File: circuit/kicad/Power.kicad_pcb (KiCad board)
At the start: 2 copper layers, 78.8 x 54.8 mm, 66 parts, among them J1 ILG2, J2 PA3, J3 FFC4, J4 FFC7, J5 PA2, J6 PA2, Q1 CXDM4060P, SW1 SW_DPDT_x2, SW2 220AMB16R, SW3 SKRPABE010, SW4 SKRPABE010, SW5 SKRPABE010, U1 AZ1117R-5.0TRE1, U2 AZ1117IH-3.3TRG1, U3 DRV8874, U4 DRV8874

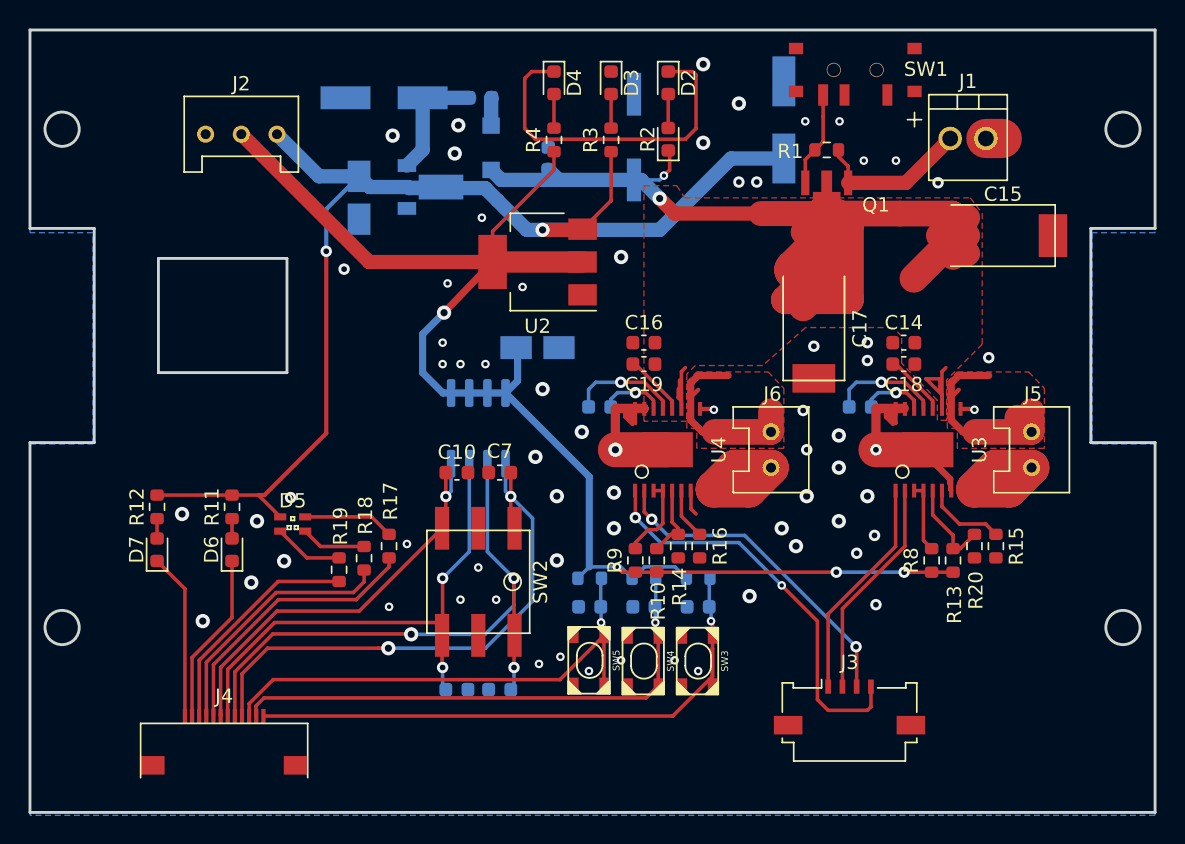
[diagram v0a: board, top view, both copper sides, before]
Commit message: フットプリントの問題は解消
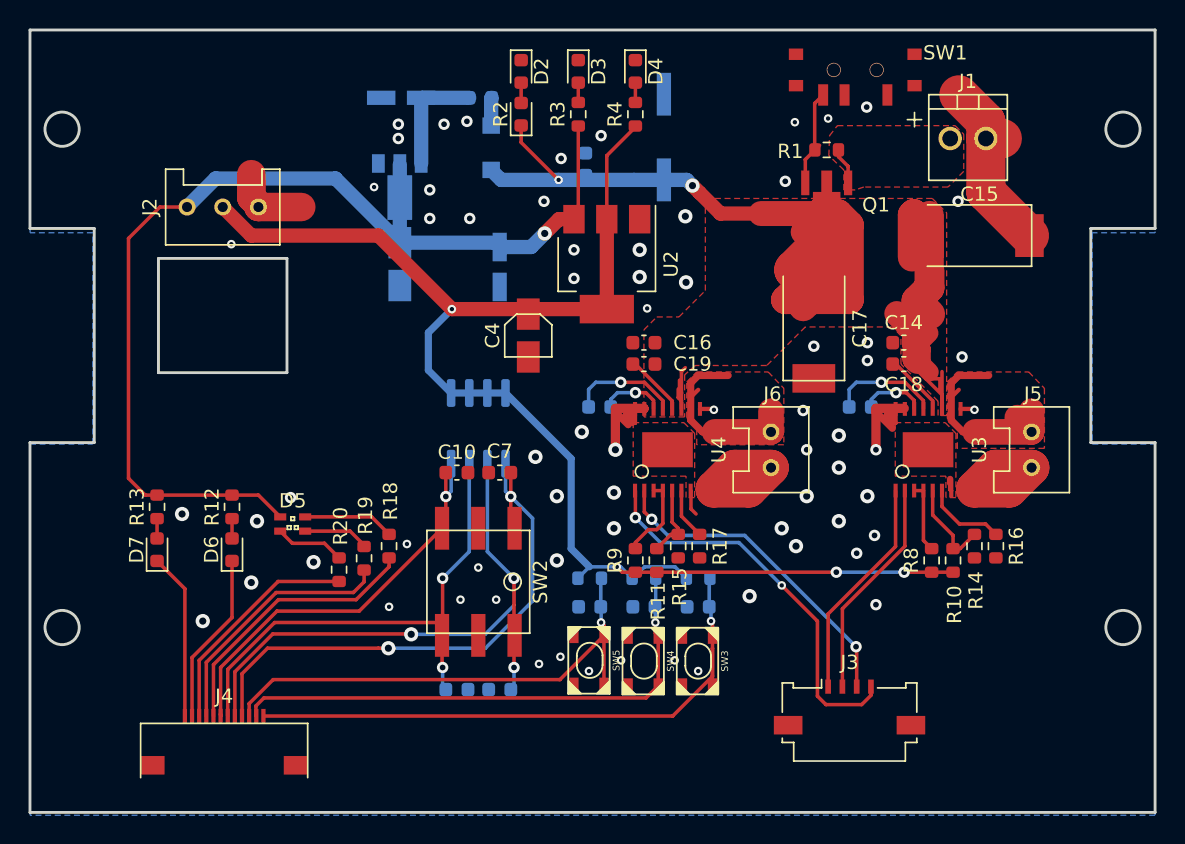
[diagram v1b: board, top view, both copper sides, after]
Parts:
- C4: moved to F.Cu
- moved C3 22.4 mm to (-6.50, -10.8), turned to 90 degrees
- moved R2 10.4 mm to (-5.00, -21.5)
- moved D2 10.3 mm to (-5.00, -24.5)
- moved R4 5.98 mm to (3.00, -21.5)
- moved D4 5.76 mm to (3.00, -24.5)
- moved C2 5.45 mm to (-13.5, -11.0)
- moved J2 5.26 mm to (-25.9, -15.0), turned to 180 degrees
- moved U2 4.85 mm to (1.00, -11.0), turned to 270 degrees
- moved R3 2.92 mm to (-1.00, -21.5)
- moved C6 2.63 mm to (-0.50, -18.0)
- moved D3 2.44 mm to (-1.00, -24.5)
- moved U1 2.15 mm to (-13.5, -16.4), turned to 270 degrees
- moved C5 2.10 mm to (5.00, -19.9)
- moved C15 1.65 mm to (27.1, -13.0)
- moved C1 1.20 mm to (-13.4, -22.6)
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- renumbered R13 to R10, R10 to R11, R11 to R12, R12 to R13, R20 to R14, R14 to R15, R15 to R16, R16 to R17, R17 to R18, R18 to R19, R19 to R20
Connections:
- SW1 pad MP: (no net) -> GND
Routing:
- net GND: track 57.0 -> 47.7 mm, vias 67 -> 68
- net Net-(J1-Pad2): track 11.0 -> 2.59 mm
- net +5V: track 84.2 -> 76.4 mm, vias 2 -> 1
- net +3V3: track 104.1 -> 101.8 mm
- net Net-(D4-Pad2): track 2.39 -> 1.39 mm
- net Net-(D3-Pad2): track 2.39 -> 1.39 mm
- net Net-(D2-Pad2): track 2.43 -> 1.42 mm
- net /DRV2_EN: track 28.7 -> 27.8 mm
- net Net-(C1-Pad1): track 8.47 -> 7.90 mm
- added copper zone on F.Cu, net Net-(J1-Pad2)

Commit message: 後はガーバデータ出してロゴ刺すだけ
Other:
- rule via_min_size: 0.4 -> 0.6
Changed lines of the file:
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@@
     (via_size 0.8)
     (via_drill 0.4)
-    (via_min_size 0.4)
+    (via_min_size 0.6)
     (via_min_drill 0.3)
     (user_via 0.6 0.3)
@@
     (pcbplotparams
       (layerselection 0x010fc_ffffffff)
-      (usegerberextensions false)
-      (usegerberattributes true)
-      (usegerberadvancedattributes true)
-      (creategerberjobfile true)
+      (usegerberextensions true)
+      (usegerberattributes false)
+      (usegerberadvancedattributes false)
+      (creategerberjobfile false)
       (excludeedgelayer true)
       (linewidth 0.100000)
@@
       (plotinvisibletext false)
       (padsonsilk false)
-      (subtractmaskfromsilk false)
+      (subtractmaskfromsilk true)
       (outputformat 1)
       (mirror false)
       (drillshape 0)
       (scaleselection 1)
-      (outputdirectory "gerver/"))
+      (outputdirectory "Gerber"))
   )
   (net 0 "")
